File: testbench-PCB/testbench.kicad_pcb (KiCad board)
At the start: 2 copper layers, 185.4 x 134.6 mm, 97 parts, among them J1 USB_C_Receptacle_USB2.0, J2 AVR-ISP, J3 AVR-JTAG, SW1 SW_Push, U1 ATmega2561-16A, U10 CH340C, U2 Thermistor_module, U3 Rotary_encoder_switch_module, U4 RTC_EEPROM_module, U6 Relay_module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

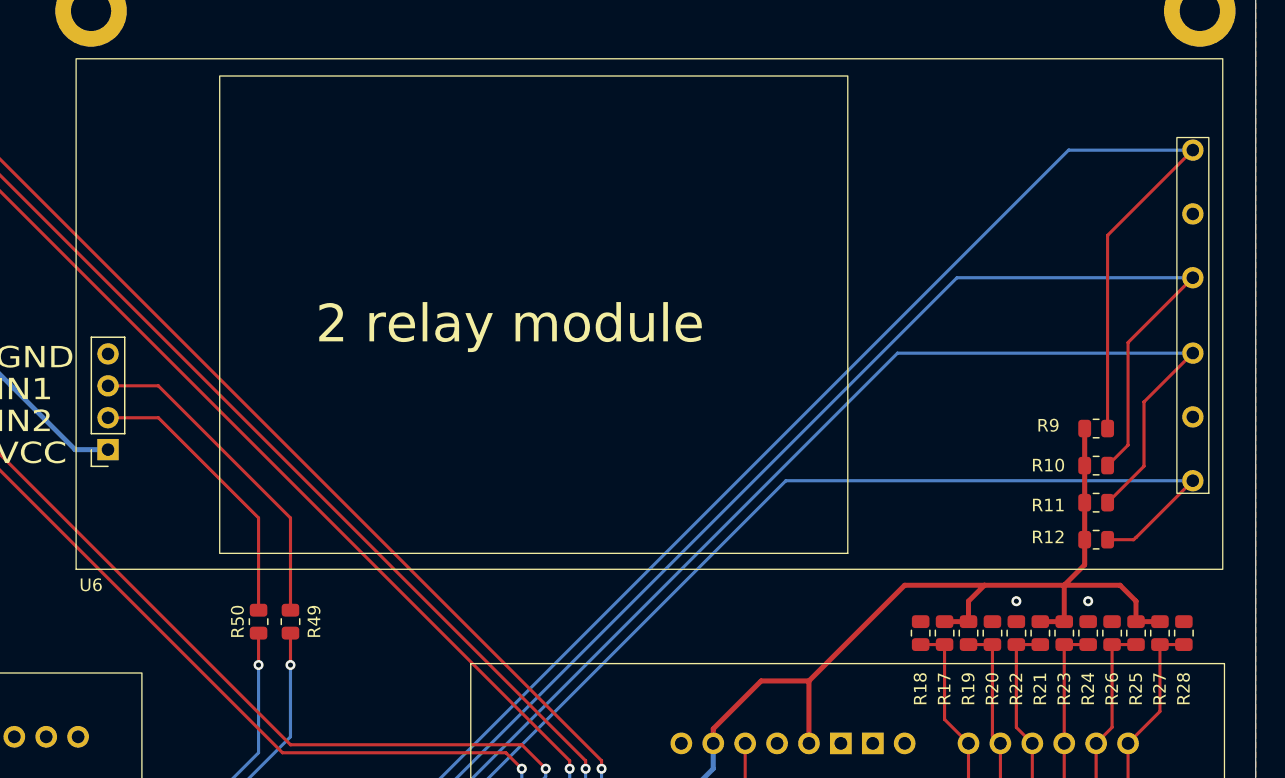
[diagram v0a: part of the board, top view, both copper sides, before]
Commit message: Edited relay module output pins.
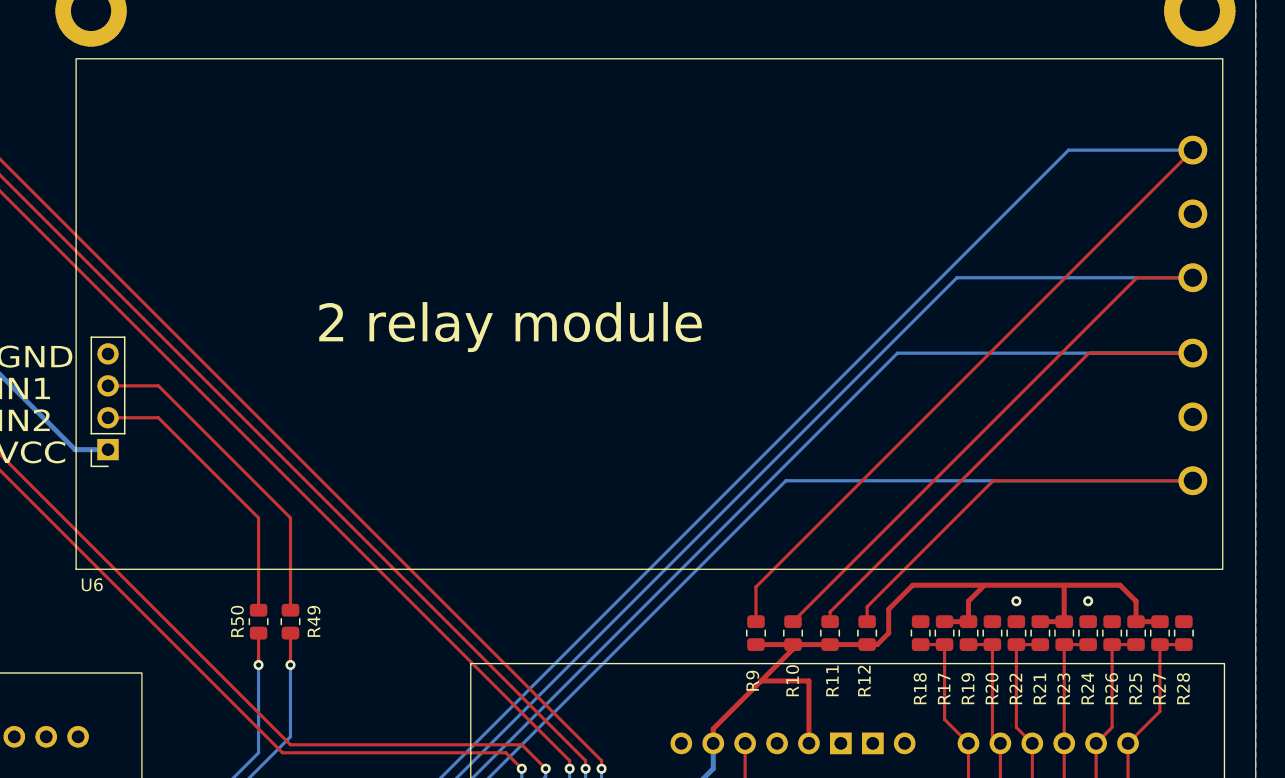
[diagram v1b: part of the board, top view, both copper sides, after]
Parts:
- moved R9 31.6 mm to (183.7, 81.3), turned to 90 degrees
- moved R10 27.6 mm to (186.7, 81.3), turned to 90 degrees
- moved R11 23.6 mm to (189.6, 81.3), turned to 90 degrees
- moved R12 19.7 mm to (192.6, 81.3), turned to 90 degrees
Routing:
- net /Kit modules/K1-NC: track 242.8 -> 269.8 mm
- net /Kit modules/K1-NO: track 228.0 -> 253.4 mm
- net /Kit modules/K2-NC: track 209.0 -> 232.4 mm
- net /Kit modules/K2-NO: track 197.4 -> 220.0 mm
- net +5V: track 634.3 -> 629.3 mm
